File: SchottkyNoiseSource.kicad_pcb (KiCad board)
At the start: 2 copper layers, 43 x 54 mm, 42 parts, among them J1 Conn_Coaxial, J2 Conn_01x02, J3 Conn_01x02, J4 Conn_Coaxial, J5 Conn_01x02, J6 Conn_Coaxial

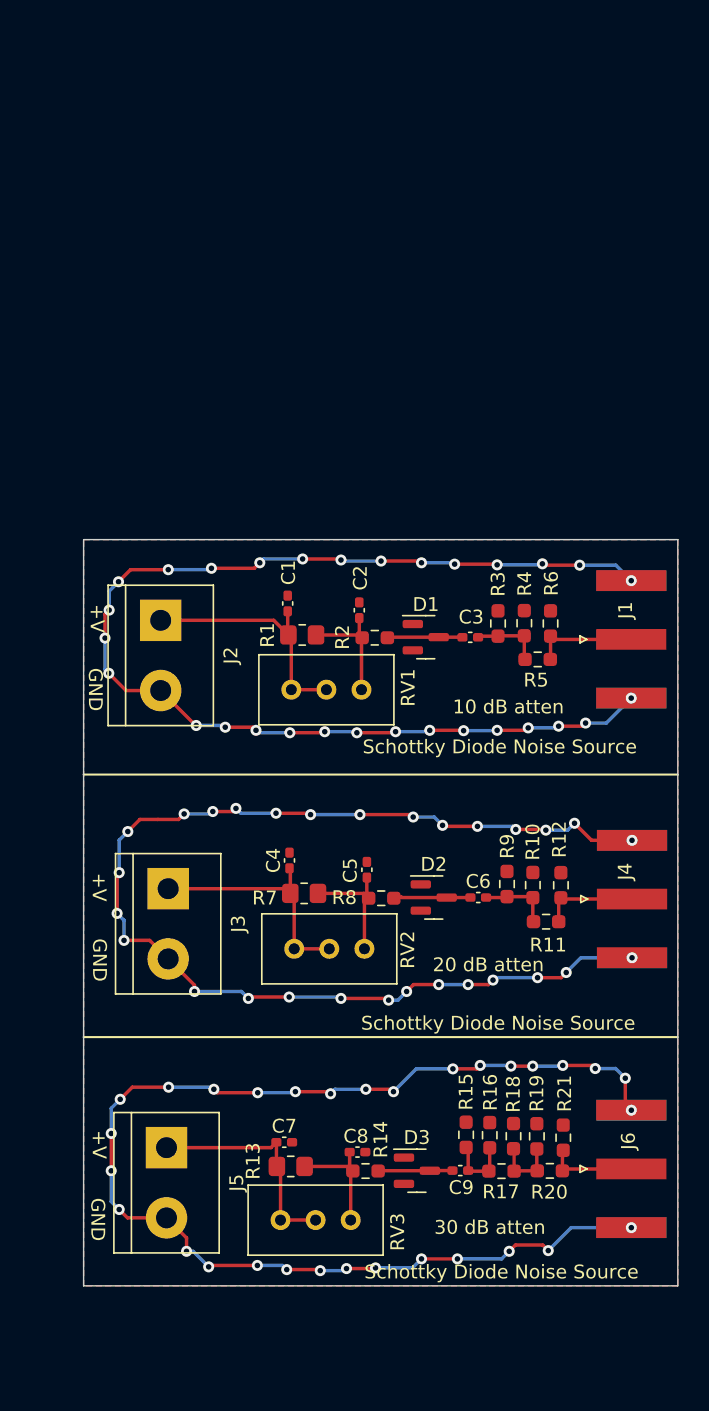
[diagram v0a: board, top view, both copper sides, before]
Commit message: Rearranged components slightly, removed solder mask to allow shield to be fitted
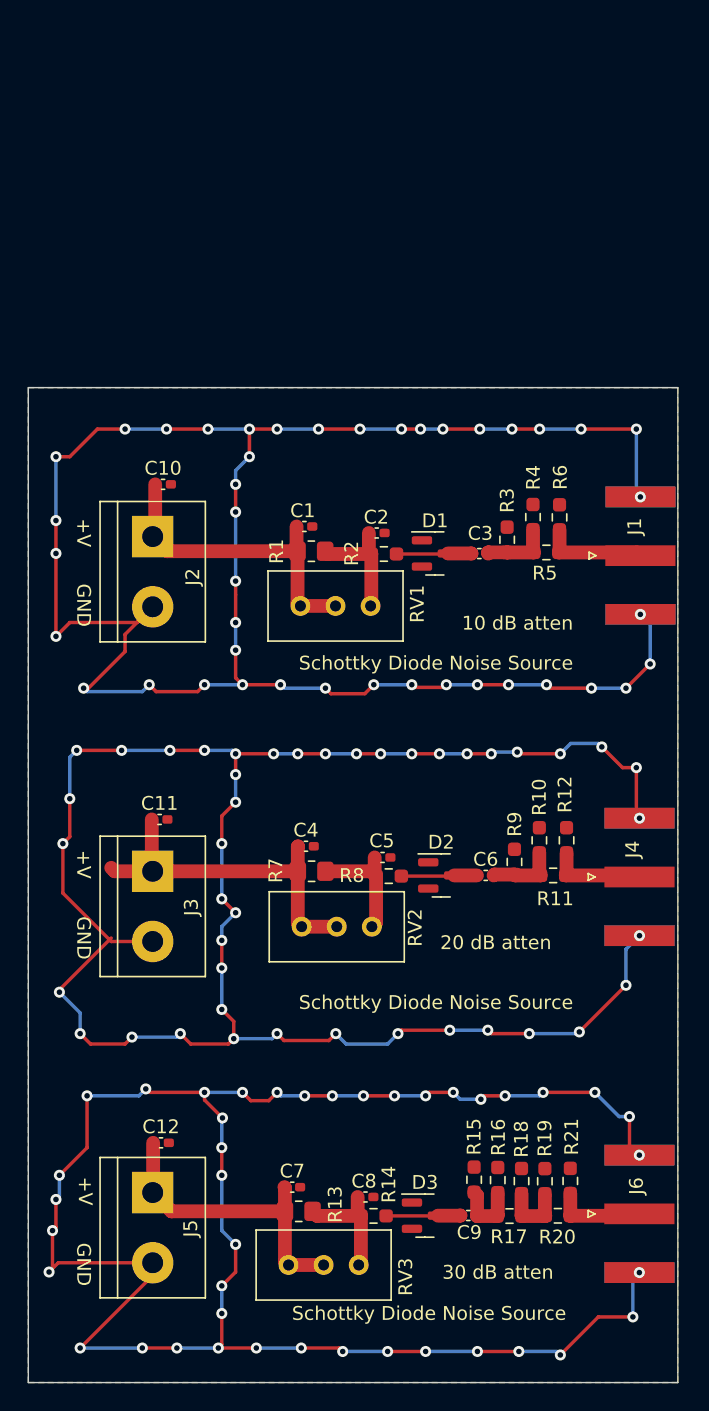
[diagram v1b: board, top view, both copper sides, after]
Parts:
- added C10: 100 nF, Capacitor_SMD:C_0402_1005Metric_Pad0.74x0.62mm_HandSolder, F.Cu at (99.8, 79.0)
- added C11: 100 nF, Capacitor_SMD:C_0402_1005Metric_Pad0.74x0.62mm_HandSolder, F.Cu at (99.5, 103.2)
- added C12: 100 nF, Capacitor_SMD:C_0402_1005Metric_Pad0.74x0.62mm_HandSolder, F.Cu at (99.6, 126.7)
- moved R5 7.77 mm to (127.5, 83.9)
- moved R6 7.71 mm to (128.4, 81.4)
- moved R4 7.71 mm to (126.5, 81.4)
- moved R1 6.10 mm to (110.5, 83.8)
- moved D1 6.10 mm to (119.4, 84.0)
- moved J1 6.10 mm to (134.3, 84.2)
- moved RV1 6.10 mm to (114.8, 87.8)
- moved R2 6.10 mm to (115.7, 84.0)
- moved R3 6.10 mm to (124.7, 83.0)
- moved C3 6.10 mm to (122.6, 84.0)
- moved J2 6.09 mm to (99.0, 82.8)
- moved C2 5.73 mm to (115.2, 82.5), turned to 0 degrees
- moved C1 5.70 mm to (110.0, 82.0), turned to 0 degrees
- moved J5 3.40 mm to (99.0, 130.2)
- moved R11 3.39 mm to (128.0, 107.3)
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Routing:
- net GND: track 264.2 -> 425.3 mm, vias 90 -> 126
- net Net-(C4-Pad1): track 17.5 -> 25.9 mm
- net Net-(C7-Pad1): track 16.4 -> 22.0 mm
- net Net-(C1-Pad1): track 18.0 -> 23.2 mm
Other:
- board size 43 x 54 mm -> 47 x 72 mm

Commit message: Added sense diode to noise sources
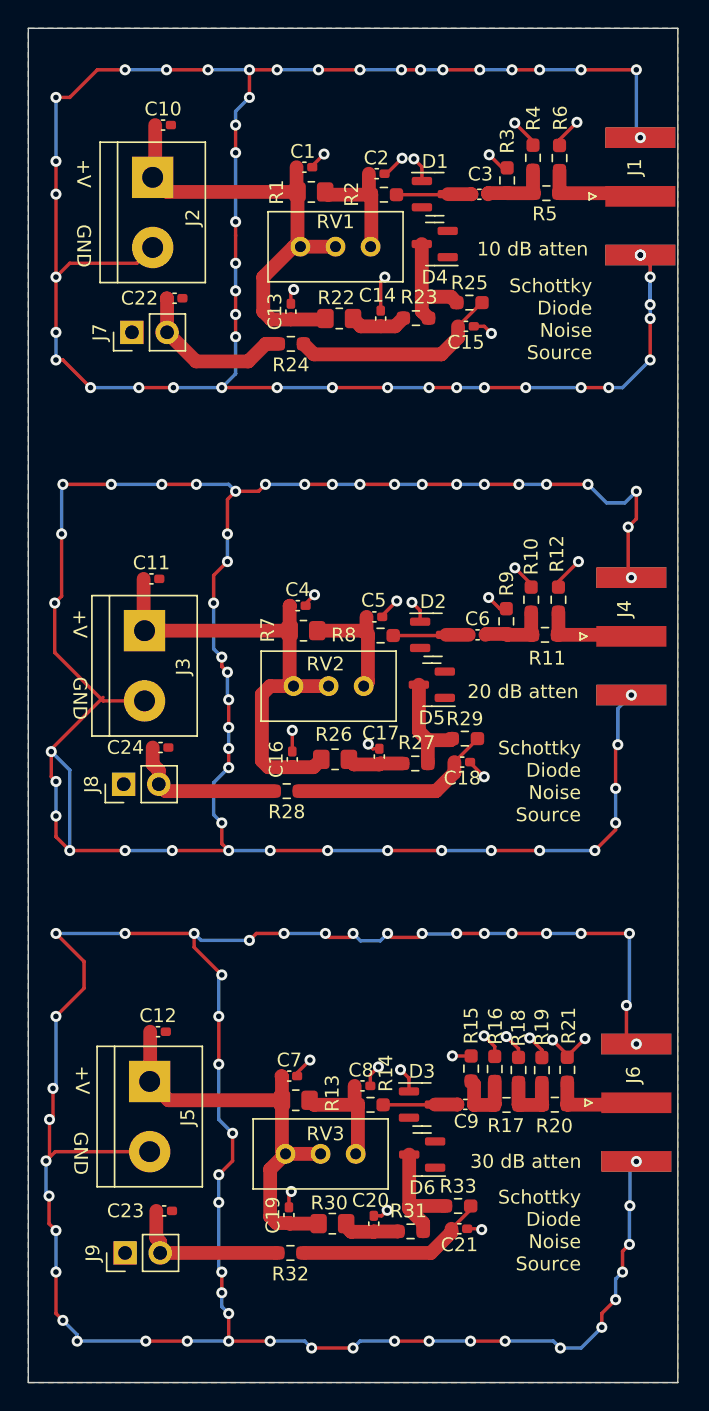
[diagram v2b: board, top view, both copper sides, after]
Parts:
- added C13: 100 nF, Capacitor_SMD:C_0402_1005Metric_Pad0.74x0.62mm_HandSolder, F.Cu at (109.0, 66.5)
- added C14: 100 nF, Capacitor_SMD:C_0402_1005Metric_Pad0.74x0.62mm_HandSolder, F.Cu at (115.5, 67.0)
- added C15: 100 nF, Capacitor_SMD:C_0402_1005Metric_Pad0.74x0.62mm_HandSolder, F.Cu at (121.7, 67.6)
- added C16: 100 nF, Capacitor_SMD:C_0402_1005Metric_Pad0.74x0.62mm_HandSolder, F.Cu at (109.1, 98.9)
- added C17: 100 nF, Capacitor_SMD:C_0402_1005Metric_Pad0.74x0.62mm_HandSolder, F.Cu at (115.4, 98.7)
- added C18: 100 nF, Capacitor_SMD:C_0402_1005Metric_Pad0.74x0.62mm_HandSolder, F.Cu at (121.4, 99.1)
- added C19: 100 nF, Capacitor_SMD:C_0402_1005Metric_Pad0.74x0.62mm_HandSolder, F.Cu at (108.9, 131.9)
- added C20: 100 nF, Capacitor_SMD:C_0402_1005Metric_Pad0.74x0.62mm_HandSolder, F.Cu at (115.0, 132.5)
- added C21: 100 nF, Capacitor_SMD:C_0402_1005Metric_Pad0.74x0.62mm_HandSolder, F.Cu at (121.2, 132.9)
- added C22: 100 nF, Capacitor_SMD:C_0402_1005Metric_Pad0.74x0.62mm_HandSolder, F.Cu at (100.6, 65.5)
- added C23: 100 nF, Capacitor_SMD:C_0402_1005Metric_Pad0.74x0.62mm_HandSolder, F.Cu at (99.8, 131.6)
- added C24: 100 nF, Capacitor_SMD:C_0402_1005Metric_Pad0.74x0.62mm_HandSolder, F.Cu at (99.6, 98.0)
- added D4: BAT17, Package_TO_SOT_SMD:SOT-23, F.Cu at (119.4, 61.6)
- added D5: BAT17, Package_TO_SOT_SMD:SOT-23, F.Cu at (119.2, 93.5)
- added D6: BAT17, Package_TO_SOT_SMD:SOT-23, F.Cu at (118.5, 127.5)
- added J7: Conn_01x02, Connector_PinHeader_2.54mm:PinHeader_1x02_P2.54mm_Vertical, F.Cu at (97.5, 68.0)
- added J8: Conn_01x02, Connector_PinHeader_2.54mm:PinHeader_1x02_P2.54mm_Vertical, F.Cu at (96.9, 100.7)
- added J9: Conn_01x02, Connector_PinHeader_2.54mm:PinHeader_1x02_P2.54mm_Vertical, F.Cu at (97.0, 134.6)
- added R22: 300R, Resistor_SMD:R_0805_2012Metric_Pad1.20x1.40mm_HandSolder, F.Cu at (112.5, 67.0)
- added R23: 3k3, Resistor_SMD:R_0603_1608Metric_Pad0.98x0.95mm_HandSolder, F.Cu at (118.0, 67.0)
- added R24: 3k3, Resistor_SMD:R_0603_1608Metric_Pad0.98x0.95mm_HandSolder, F.Cu at (109.0, 68.8)
- added R25: 3k3, Resistor_SMD:R_0603_1608Metric_Pad0.98x0.95mm_HandSolder, F.Cu at (121.9, 65.8)
- added R26: 300R, Resistor_SMD:R_0805_2012Metric_Pad1.20x1.40mm_HandSolder, F.Cu at (112.2, 98.9)
- added R27: 3k3, Resistor_SMD:R_0603_1608Metric_Pad0.98x0.95mm_HandSolder, F.Cu at (118.0, 99.2)
- added R28: 3k3, Resistor_SMD:R_0603_1608Metric_Pad0.98x0.95mm_HandSolder, F.Cu at (108.7, 101.2)
- added R29: 3k3, Resistor_SMD:R_0603_1608Metric_Pad0.98x0.95mm_HandSolder, F.Cu at (121.6, 97.4)
- added R30: 300R, Resistor_SMD:R_0805_2012Metric_Pad1.20x1.40mm_HandSolder, F.Cu at (112.0, 132.5)
- added R31: 3k3, Resistor_SMD:R_0603_1608Metric_Pad0.98x0.95mm_HandSolder, F.Cu at (117.7, 133.1)
- added R32: 3k3, Resistor_SMD:R_0603_1608Metric_Pad0.98x0.95mm_HandSolder, F.Cu at (109.0, 134.6)
- added R33: 3k3, Resistor_SMD:R_0603_1608Metric_Pad0.98x0.95mm_HandSolder, F.Cu at (121.1, 131.2)
- moved C3 26.0 mm to (122.6, 58.0)
- moved R2 26.0 mm to (115.7, 58.0)
- moved R3 26.0 mm to (124.7, 57.0)
- moved R4 26.0 mm to (126.5, 55.4)
- moved R5 26.0 mm to (127.5, 57.9)
- moved C1 26.0 mm to (110.0, 56.0)
- moved C10 26.0 mm to (99.8, 53.0)
- moved D1 26.0 mm to (119.4, 58.0)
- moved J1 26.0 mm to (134.3, 58.2)
- moved J2 26.0 mm to (99.0, 56.8)
- moved R1 26.0 mm to (110.5, 57.8)
- moved R6 26.0 mm to (128.4, 55.4)
- moved RV1 26.0 mm to (114.8, 61.8)
- moved C2 26.0 mm to (115.2, 56.5)
- moved R10 17.4 mm to (126.4, 87.3)
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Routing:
- net GND: track 425.3 -> 549.3 mm, vias 126 -> 180
- net Net-(C15-Pad2): track 0.00 -> 15.3 mm
- net Net-(C18-Pad2): track 0.00 -> 14.9 mm
- net Net-(C21-Pad2): track 0.00 -> 13.8 mm
- net Net-(R24-Pad1): track 0.00 -> 11.9 mm
- net Net-(J9-Pad2): track 0.00 -> 11.7 mm
- net Net-(R28-Pad1): track 0.00 -> 11.4 mm
- net Net-(C1-Pad1): track 23.2 -> 34.0 mm
- net Net-(C11-Pad1): track 25.9 -> 34.8 mm
- net Net-(C12-Pad1): track 22.0 -> 30.8 mm
- net Net-(D6-Pad3): track 0.00 -> 8.61 mm
- net Net-(D4-Pad3): track 0.00 -> 8.27 mm
- net Net-(D5-Pad3): track 0.00 -> 7.78 mm
- net Net-(C20-Pad1): track 0.00 -> 4.13 mm
- net Net-(C14-Pad1): track 0.00 -> 4.12 mm
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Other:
- board size 47 x 72 mm -> 47 x 98 mm

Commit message: Added heater resistors
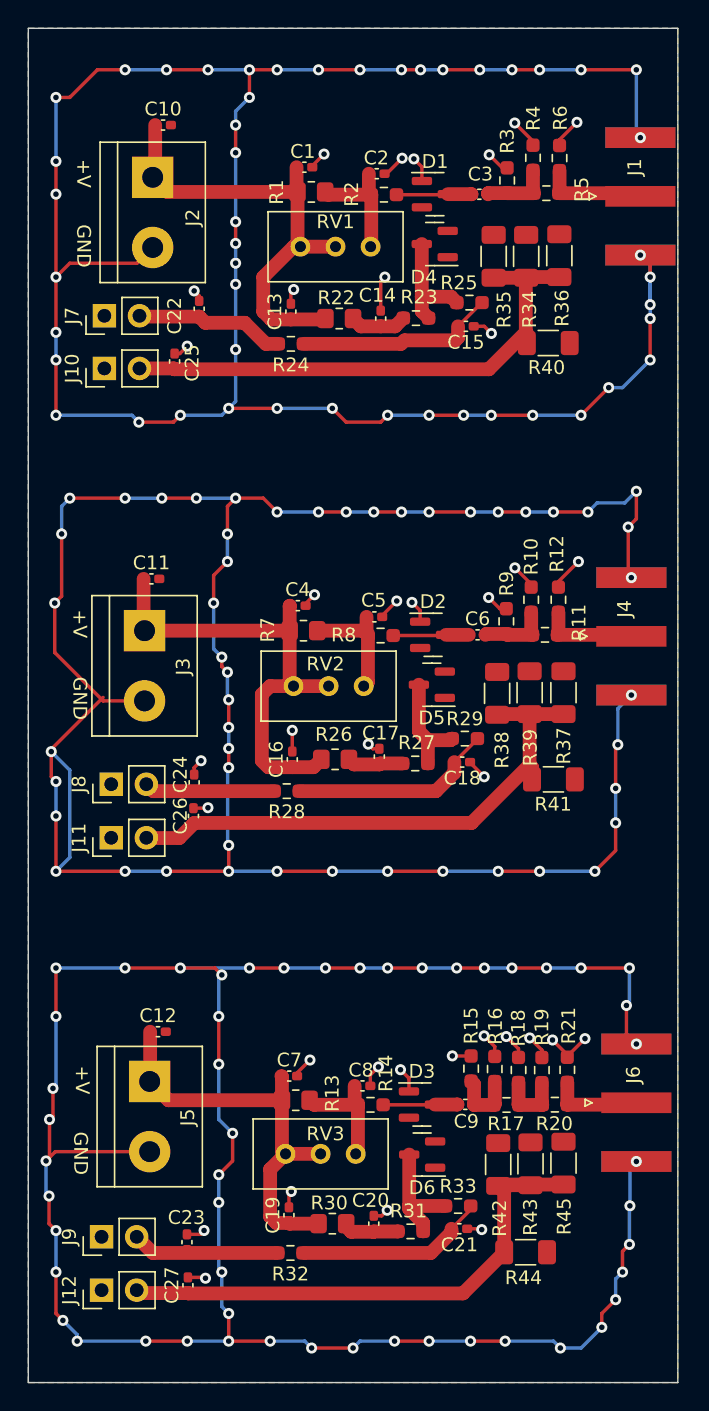
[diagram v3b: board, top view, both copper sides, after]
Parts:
- added C25: 100 nF, Capacitor_SMD:C_0402_1005Metric_Pad0.74x0.62mm_HandSolder, F.Cu at (100.6, 70.1)
- added C26: 100 nF, Capacitor_SMD:C_0402_1005Metric_Pad0.74x0.62mm_HandSolder, F.Cu at (102.0, 103.0)
- added C27: 100 nF, Capacitor_SMD:C_0402_1005Metric_Pad0.74x0.62mm_HandSolder, F.Cu at (101.5, 137.0)
- added J10: Conn_01x02, Connector_PinHeader_2.54mm:PinHeader_1x02_P2.54mm_Vertical, F.Cu at (95.5, 70.6)
- added J11: Conn_01x02, Connector_PinHeader_2.54mm:PinHeader_1x02_P2.54mm_Vertical, F.Cu at (96.0, 104.6)
- added J12: Conn_01x02, Connector_PinHeader_2.54mm:PinHeader_1x02_P2.54mm_Vertical, F.Cu at (95.3, 137.3)
- added R34: 100R, Resistor_SMD:R_1206_3216Metric_Pad1.30x1.75mm_HandSolder, F.Cu at (126.0, 62.5)
- added R35: 100R, Resistor_SMD:R_1206_3216Metric_Pad1.30x1.75mm_HandSolder, F.Cu at (123.7, 62.5)
- added R36: 100R, Resistor_SMD:R_1206_3216Metric_Pad1.30x1.75mm_HandSolder, F.Cu at (128.4, 62.5)
- added R37: 100R, Resistor_SMD:R_1206_3216Metric_Pad1.30x1.75mm_HandSolder, F.Cu at (128.7, 94.1)
- added R38: 100R, Resistor_SMD:R_1206_3216Metric_Pad1.30x1.75mm_HandSolder, F.Cu at (123.9, 94.1)
- added R39: 100R, Resistor_SMD:R_1206_3216Metric_Pad1.30x1.75mm_HandSolder, F.Cu at (126.3, 94.1)
- added R40: 100R, Resistor_SMD:R_1206_3216Metric_Pad1.30x1.75mm_HandSolder, F.Cu at (127.6, 68.8)
- added R41: 100R, Resistor_SMD:R_1206_3216Metric_Pad1.30x1.75mm_HandSolder, F.Cu at (128.0, 100.3)
- added R42: 100R, Resistor_SMD:R_1206_3216Metric_Pad1.30x1.75mm_HandSolder, F.Cu at (124.0, 128.2)
- added R43: 100R, Resistor_SMD:R_1206_3216Metric_Pad1.30x1.75mm_HandSolder, F.Cu at (126.3, 128.2)
- added R44: 100R, Resistor_SMD:R_1206_3216Metric_Pad1.30x1.75mm_HandSolder, F.Cu at (126.0, 134.6)
- added R45: 100R, Resistor_SMD:R_1206_3216Metric_Pad1.30x1.75mm_HandSolder, F.Cu at (128.7, 128.1)
- moved C24 3.50 mm to (102.0, 100.6), turned to -90 degrees
- moved C23 2.80 mm to (101.5, 133.8), turned to -90 degrees
- moved J7 2.33 mm to (95.5, 66.8)
- moved J9 2.06 mm to (95.3, 133.5)
- moved C22 1.93 mm to (102.4, 66.3), turned to -90 degrees
- moved J8 0.90 mm to (96.0, 100.7)
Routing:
- net Net-(C27-Pad1): track 0.00 -> 40.0 mm
- net Net-(C26-Pad1): track 0.00 -> 39.6 mm
- net Net-(C25-Pad1): track 0.00 -> 38.6 mm
- net GND: track 549.3 -> 557.2 mm, vias 180 -> 184
- net Net-(C24-Pad2): track 11.4 -> 9.45 mm
- net Net-(C22-Pad2): track 11.9 -> 10.9 mm
- net Net-(C23-Pad2): track 11.7 -> 10.7 mm
- net Net-(C15-Pad2): track 15.3 -> 14.6 mm

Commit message: Made pin header connector
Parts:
- J2, J3, J5: footprint TerminalBlock:TerminalBlock_bornier-2_P5.08mm -> Connector_PinHeader_2.54mm:PinHeader_1x02_P2.54mm_Vertical
- R34, R35, R36, R37, R38, R39, R40, R41, R42, R43, R44, R45: value 100R -> 4k7
- moved C12 9.74 mm to (99.8, 128.3)
- moved C11 9.28 mm to (99.7, 95.1)
- moved J5 8.89 mm to (96.5, 130.8), turned to 90 degrees
- moved J3 8.41 mm to (96.5, 97.8), turned to 90 degrees
- moved C10 8.00 mm to (99.9, 61.0)
- moved J2 7.16 mm to (96.5, 63.5), turned to 90 degrees
- moved J10 2.27 mm to (96.5, 68.6)
- moved J12 1.83 mm to (96.5, 135.9)
- moved J11 1.78 mm to (96.5, 102.9)
- moved C25 1.78 mm to (102.4, 70.1)
- moved J7 1.27 mm to (96.5, 66.0)
- moved J9 1.22 mm to (96.5, 133.5)
- moved C27 0.81 mm to (102.4, 136.9)
- moved J8 0.64 mm to (96.5, 100.3)
- moved C23 0.63 mm to (102.1, 133.8)
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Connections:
- J2 pad 1: Net-(C1-Pad1) -> GND
- J2 pad 2: GND -> Net-(C1-Pad1)
- J3 pad 1: Net-(C11-Pad1) -> GND
- J3 pad 2: GND -> Net-(C11-Pad1)
- J5 pad 1: Net-(C12-Pad1) -> GND
- J5 pad 2: GND -> Net-(C12-Pad1)
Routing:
- net GND: track 557.2 -> 624.7 mm, vias 184 -> 221
- net Net-(C11-Pad1): track 34.8 -> 36.7 mm
- net Net-(C12-Pad1): track 30.8 -> 32.3 mm
- net Net-(C23-Pad2): track 10.7 -> 9.48 mm
- net Net-(C25-Pad1): track 38.6 -> 39.6 mm
- net Net-(C26-Pad1): track 39.6 -> 40.3 mm
- net Net-(C22-Pad2): track 10.9 -> 10.2 mm
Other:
- board text added: "Drive"
- board text added: "Heat"
- board text added: "Sense"
- board text removed: "+V"
- board text removed: "GND"
